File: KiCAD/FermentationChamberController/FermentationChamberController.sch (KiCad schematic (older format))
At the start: 18 parts, among them J1 Screw_Terminal_1x02, J2 Screw_Terminal_1x02, J3 Screw_Terminal_1x02, J4 CONN_01X04, J5 CONN_01X04, P1 Digital, P2 Analog, Q1 TIP120, Q2 TIP120, SW1 Rotary_Encoder_Switch

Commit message: Updated PCB layour
almost done.... maybe
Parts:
- J1: value Screw_Terminal_1x02 -> G Vcc; footprint Connectors_Terminal_Blocks:TerminalBlock_WAGO-804_RM5mm_2pol -> Connectors:bornier2
- J2: value Screw_Terminal_1x02 -> 1Wire 1Wire; footprint Connectors_Terminal_Blocks:TerminalBlock_WAGO-804_RM5mm_2pol -> Connectors:bornier2
- J3: value Screw_Terminal_1x02 -> Vcc G; footprint Connectors_Terminal_Blocks:TerminalBlock_WAGO-804_RM5mm_2pol -> Connectors:bornier2
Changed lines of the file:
@@
 P 1000 6500
 F 0 "J1" H 1000 6750 50  0000 C TNN
-F 1 "Screw_Terminal_1x02" V 850 6500 50  0000 C TNN
-F 2 "Connectors_Terminal_Blocks:TerminalBlock_WAGO-804_RM5mm_2pol" H 1000 6275 50  0001 C CNN
+F 1 "G   Vcc" V 850 6500 50  0000 C TNN
+F 2 "Connectors:bornier2" H 1000 6275 50  0001 C CNN
 F 3 "" H 975 6500 50  0001 C CNN
 	1    1000 6500
@@
 P 1850 6500
 F 0 "J2" H 1850 6750 50  0000 C TNN
-F 1 "Screw_Terminal_1x02" V 1700 6500 50  0000 C TNN
-F 2 "Connectors_Terminal_Blocks:TerminalBlock_WAGO-804_RM5mm_2pol" H 1850 6275 50  0001 C CNN
+F 1 "1Wire 1Wire" V 1700 6500 50  0000 C TNN
+F 2 "Connectors:bornier2" H 1850 6275 50  0001 C CNN
 F 3 "" H 1825 6500 50  0001 C CNN
 	1    1850 6500
@@
 P 2700 6500
 F 0 "J3" H 2700 6750 50  0000 C TNN
-F 1 "Screw_Terminal_1x02" V 2550 6500 50  0000 C TNN
-F 2 "Connectors_Terminal_Blocks:TerminalBlock_WAGO-804_RM5mm_2pol" H 2700 6275 50  0001 C CNN
+F 1 "Vcc  G" V 2550 6500 50  0000 C TNN
+F 2 "Connectors:bornier2" H 2700 6275 50  0001 C CNN
 F 3 "" H 2675 6500 50  0001 C CNN
 	1    2700 6500

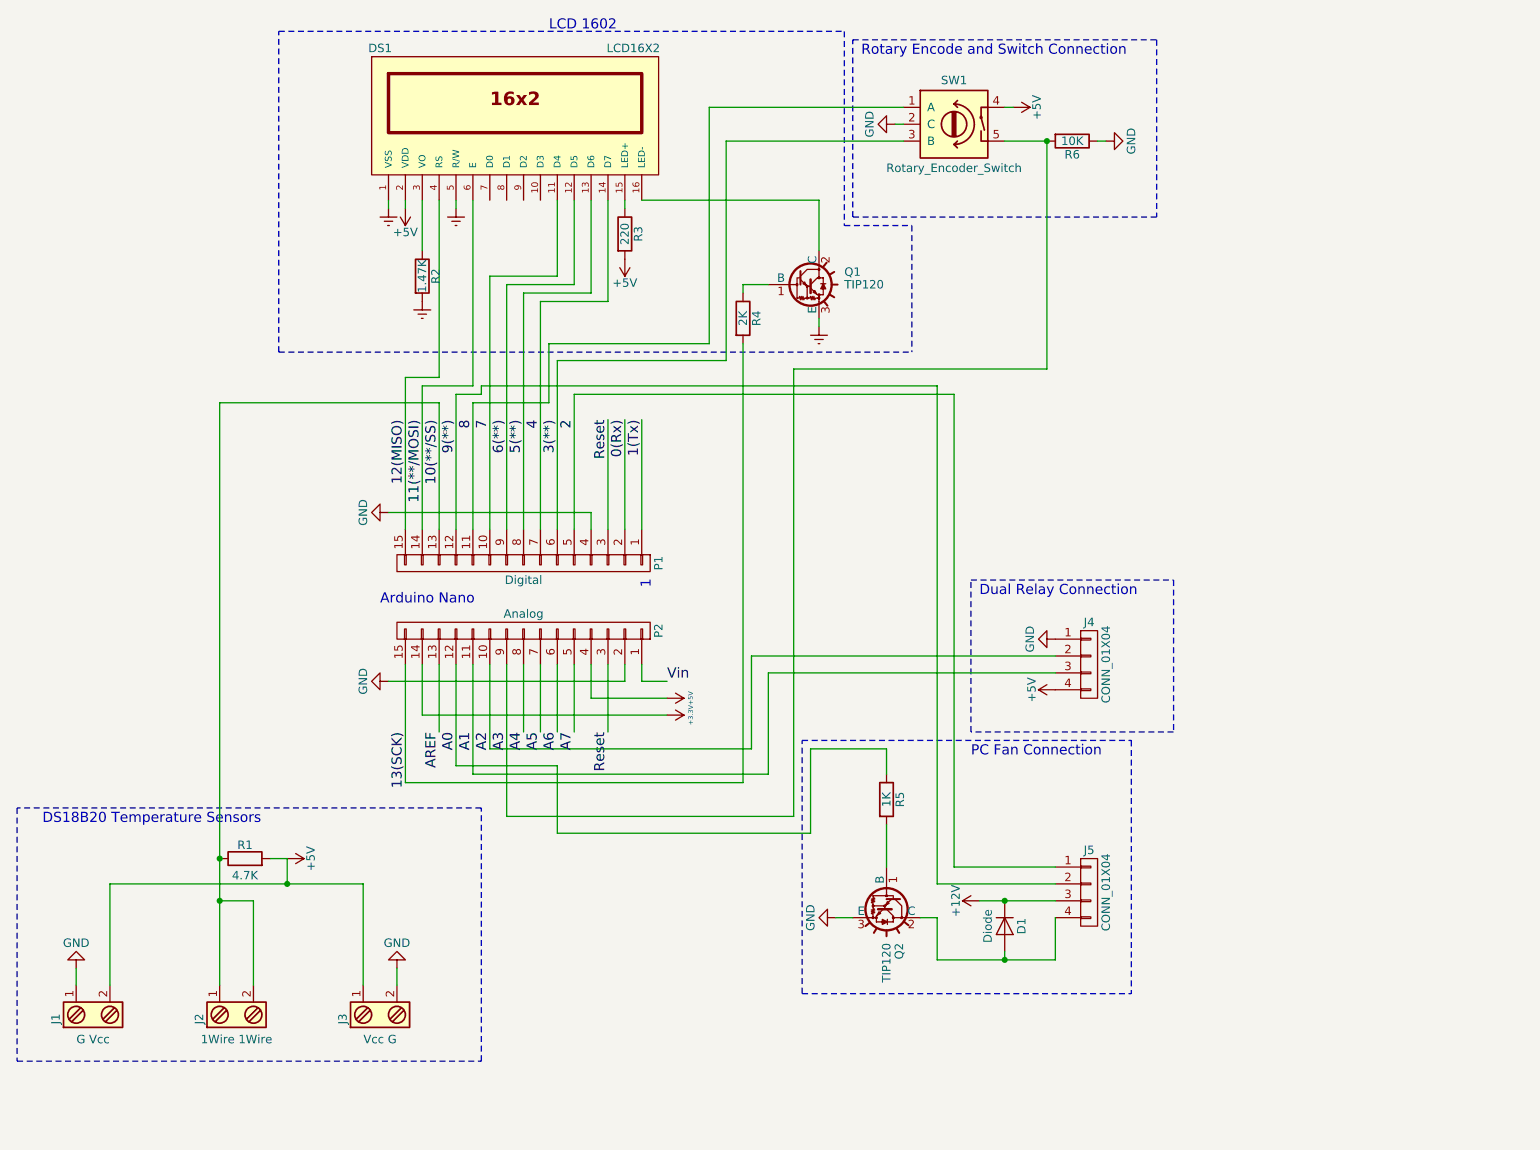
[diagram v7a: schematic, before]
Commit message: Updated schematic to split into two pcbs
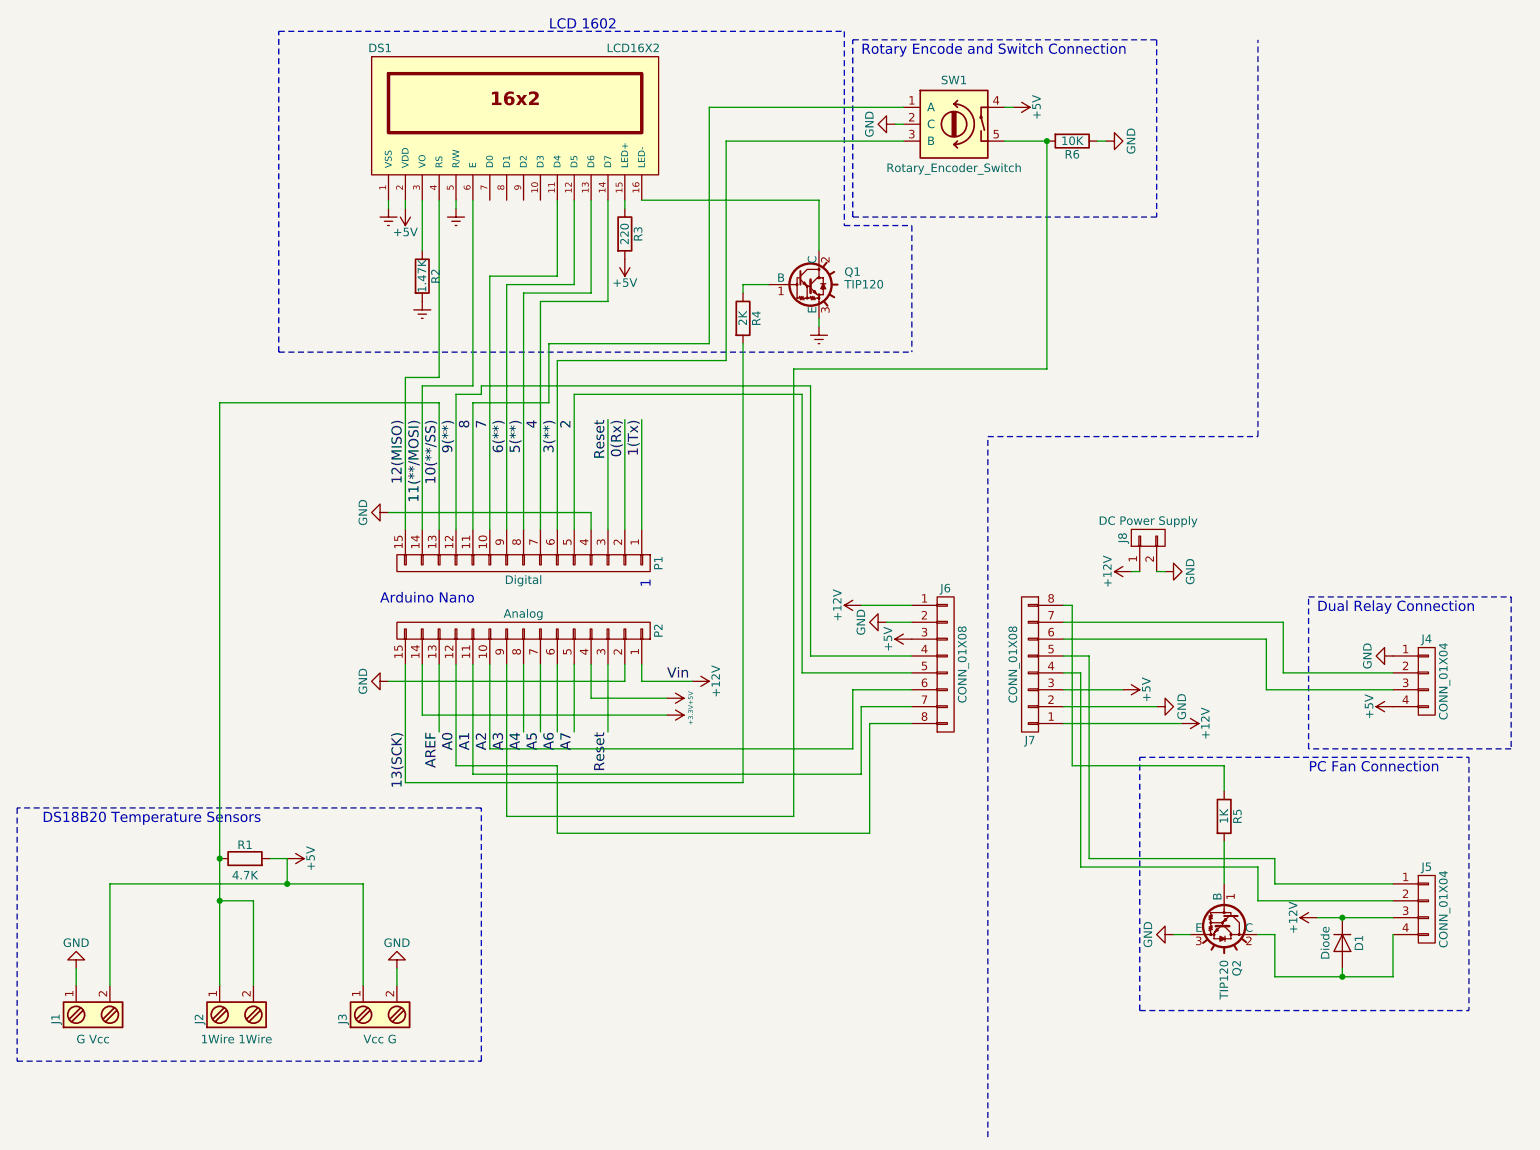
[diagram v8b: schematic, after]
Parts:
- added J6, J7: CONN_01X08, symbol CONN_01X08
- added J8: DC Power Supply, symbol CONN_01X02
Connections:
- net Vin is gone; now on net +12V: P2.1 (P1)
- net +12V: now also J6.1 (P1), J7.1 (P1), J8.1 (P1)
- net +5V: now also J6.3 (P3), J7.3 (P3)
- net 2: now also J6.5 (P5); no longer J5.1 (P1)
- net 9(**): now also J6.4 (P4); no longer J5.2 (P2)
- net A0: now also J6.8 (P8); no longer R5.1
- net A1: now also J6.7 (P7); no longer J4.3 (P3)
- net A2: now also J6.6 (P6); no longer J4.2 (P2)
- net GND: now also J6.2 (P2), J7.2 (P2), J8.2 (P2)
- new net: J5.1 (P1), J7.5 (P5)
- new net: J5.2 (P2), J7.4 (P4)
- new net: J4.2 (P2), J7.7 (P7)
- new net: J4.3 (P3), J7.6 (P6)
- new net: J7.8 (P8), R5.1
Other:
- moved on the sheet: D1, J4, J5, Q2, R5
